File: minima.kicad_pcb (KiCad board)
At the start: 2 copper layers, 84 x 60 mm, 40 parts, among them J1 output, J2 input, J3 powersupply, U1 LM1875

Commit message: Release version v1.1
Signed-off-by: Nenad Radulovic <nenad.b.radulovic@gmail.com>
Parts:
- moved LOGO1 33.9 mm to (110.5, 64.2), turned to 270 degrees
- moved J2 13.1 mm to (120.2, 97.2)
- moved C4 11.2 mm to (117.0, 69.3)
- moved C14 9.86 mm to (120.8, 82.0)
- moved R11 9.86 mm to (113.2, 85.2)
- moved R12 9.86 mm to (113.2, 78.8)
- moved C13 9.86 mm to (120.8, 88.3)
- moved R10 9.86 mm to (120.8, 91.5)
- moved J1 3.36 mm to (165.2, 99.8)
- moved L1 3.24 mm to (155.1, 58.5)
- moved R6 3.18 mm to (170.3, 50.2)
- moved MK1 3.00 mm to (112.6, 99.7)
- moved MK2 3.00 mm to (112.6, 51.7)
- moved MK3 3.00 mm to (178.6, 51.7)
- moved MK4 3.00 mm to (178.6, 99.7)
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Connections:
- J2 pad 2: GNDPWR -> /Input amplifier/sgnd
- J2 pad 3: /Input amplifier/sgnd -> GNDPWR
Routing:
- net /Input amplifier/sgnd: track 61.4 -> 83.2 mm
- net Net-(C10-Pad1): track 102.0 -> 112.4 mm
- net VCC: track 52.3 -> 42.0 mm, vias 0 -> 1
- net Net-(C4-Pad1): track 19.2 -> 10.8 mm
- net /Input amplifier/inp: track 5.91 -> 10.8 mm
- net VEE: track 56.0 -> 53.5 mm
- net /Power amplifier/inp: track 21.9 -> 24.1 mm
- net GNDPWR: track 110.7 -> 109.0 mm
- net /Power amplifier/spkhot: track 53.6 -> 54.6 mm
- net Net-(C7-Pad1): track 10.1 -> 11.1 mm
- net Net-(C3-Pad1): track 4.45 -> 3.81 mm
- net Net-(C2-Pad1): track 4.38 -> 3.81 mm
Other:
- board size 84 x 60 mm -> 78 x 60 mm
- board text added: "+|SG|G"
- board text added: "20180801-1.1"
- board text added: "Minima V1.1"
- board text removed: "+|G|SG"
- board text removed: "01.08.2018 1.0"
- board text removed: "Minima V1.0"

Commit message: Switching to single sch sheet 1
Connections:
- net /Input amplifier/inp renamed /inp
- net /Input amplifier/sgnd renamed /sgnd
- net /Power amplifier/inp renamed Net-(C14-Pad1)
- net /Power amplifier/spkhot renamed /spkhot

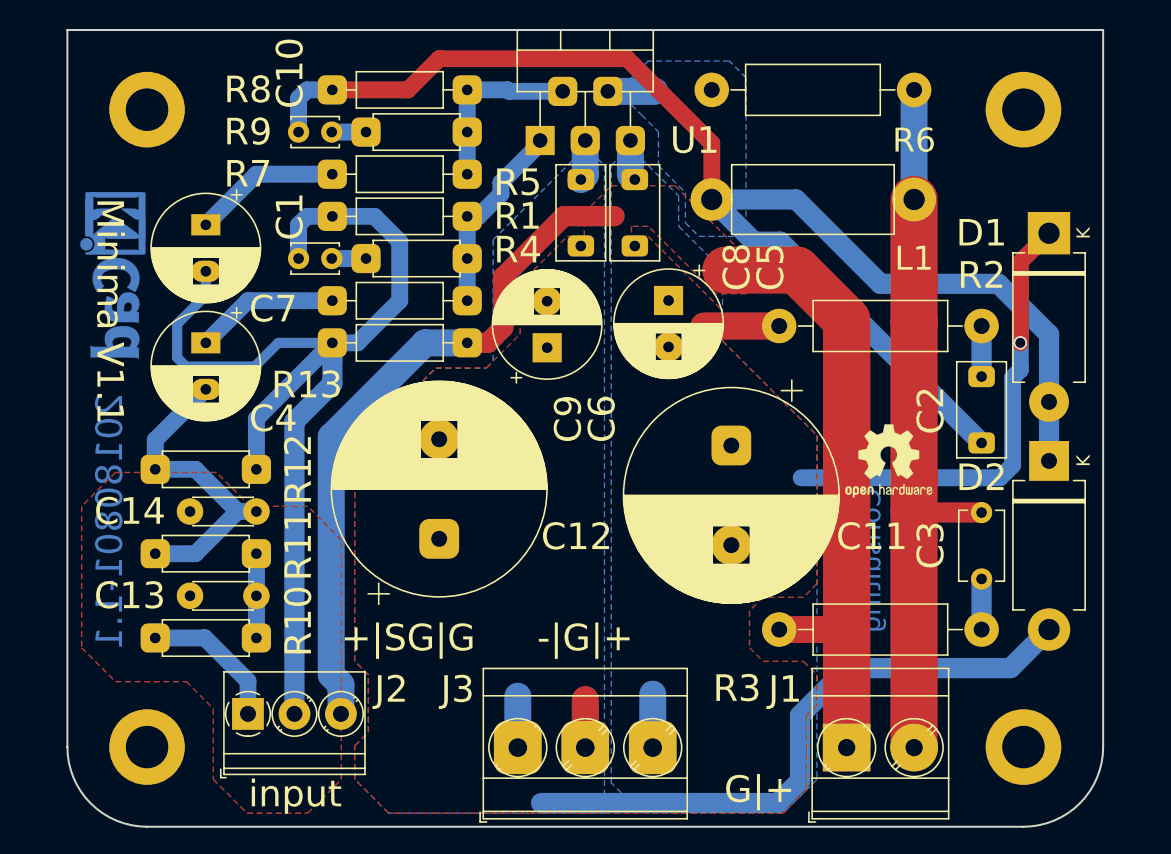
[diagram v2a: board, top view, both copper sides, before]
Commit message: Removed sheets
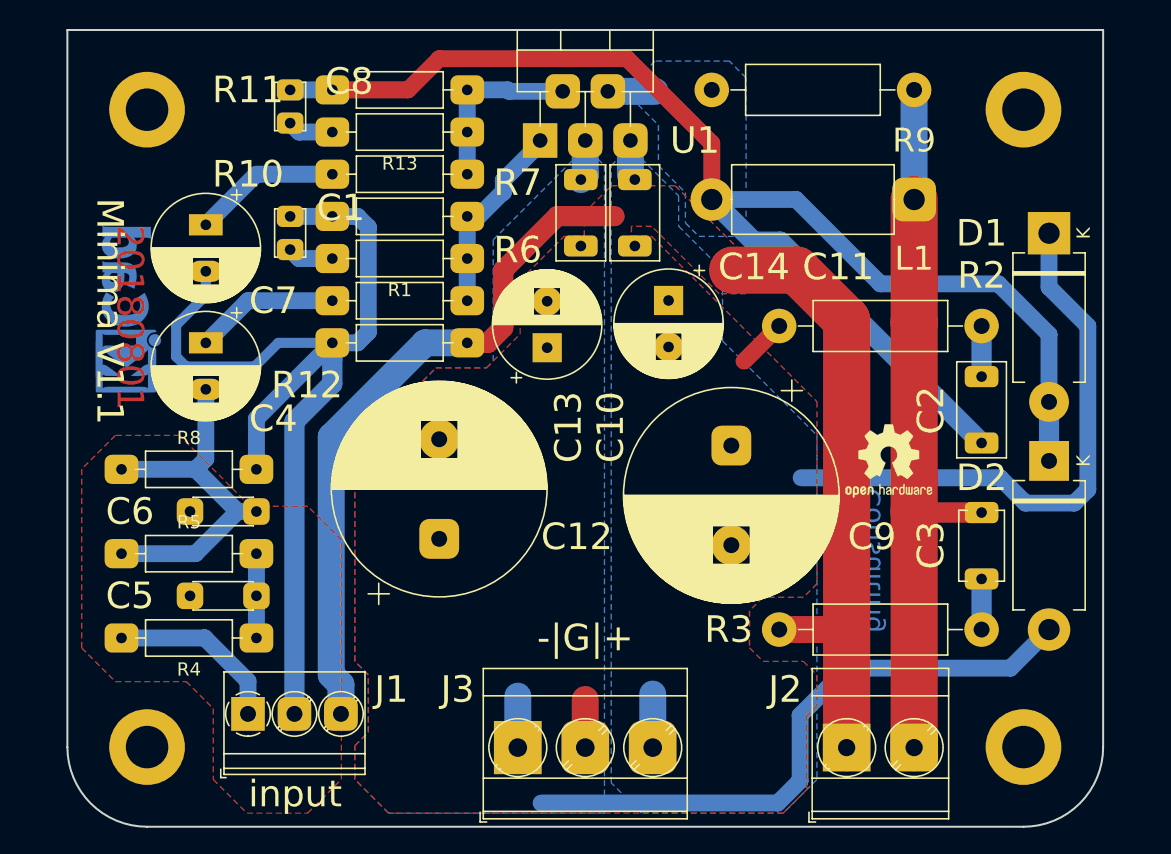
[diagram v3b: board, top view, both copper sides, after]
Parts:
- removed the C10 at (124.0, 53.4)
- removed the R10 at (120.8, 91.5)
- removed the R11 at (113.2, 85.2)
- removed the R12 at (113.2, 78.8)
- removed the R9 at (136.7, 53.4)
- added C8: 15p, Capacitor_THT:C_Disc_D3.4mm_W2.1mm_P2.50mm, F.Cu at (123.3, 50.2)
- added R13: 1k6, Resistor_THT:R_Axial_DIN0207_L6.3mm_D2.5mm_P10.16mm_Horizontal, F.Cu at (136.7, 53.4)
- added R4: 100, Resistor_THT:R_Axial_DIN0207_L6.3mm_D2.5mm_P10.16mm_Horizontal, F.Cu at (120.8, 91.5)
- added R5: 100, Resistor_THT:R_Axial_DIN0207_L6.3mm_D2.5mm_P10.16mm_Horizontal, F.Cu at (110.6, 85.2)
- added R8: 100k, Resistor_THT:R_Axial_DIN0207_L6.3mm_D2.5mm_P10.16mm_Horizontal, F.Cu at (110.6, 78.8)
- R1: footprint Resistor_THT:R_Axial_DIN0207_L6.3mm_D2.5mm_P7.62mm_Horizontal -> Resistor_THT:R_Axial_DIN0207_L6.3mm_D2.5mm_P10.16mm_Horizontal
- moved C1 3.24 mm to (123.3, 59.8), turned to 270 degrees
- moved LOGO1 2.54 mm to (110.6, 66.7), turned to 90 degrees
- renumbered C6 to C10, C5 to C11, C9 to C13, C8 to C14, C13 to C5, C14 to C6, C11 to C9, J2 to J1, J1 to J2, R7 to R10, R8 to R11, R13 to R12, R4 to R6, R5 to R7, R6 to R9
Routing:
- net VCC: track 42.0 -> 50.4 mm, vias 1 -> 0
- net /sgnd: track 83.2 -> 78.4 mm
- net Net-(C4-Pad2): track 24.1 -> 27.9 mm
- net Net-(C8-Pad2): track 0.00 -> 3.45 mm
- net Net-(C10-Pad2): track 2.58 -> 0.00 mm
- net /inp: track 10.8 -> 13.4 mm
- net Net-(C2-Pad2): track 112.4 -> 110.2 mm
- net GNDPWR: track 109.0 -> 106.8 mm
- net Net-(C1-Pad2): track 2.58 -> 3.45 mm
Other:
- board text added: "20180801"
- board text removed: "+|SG|G"
- board text removed: "20180801-1.1"
- board text removed: "G|+"

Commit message: Wider pads and some final touches to silkscreen.
Signed-off-by: Nenad Radulovic <nenad.b.radulovic@gmail.com>
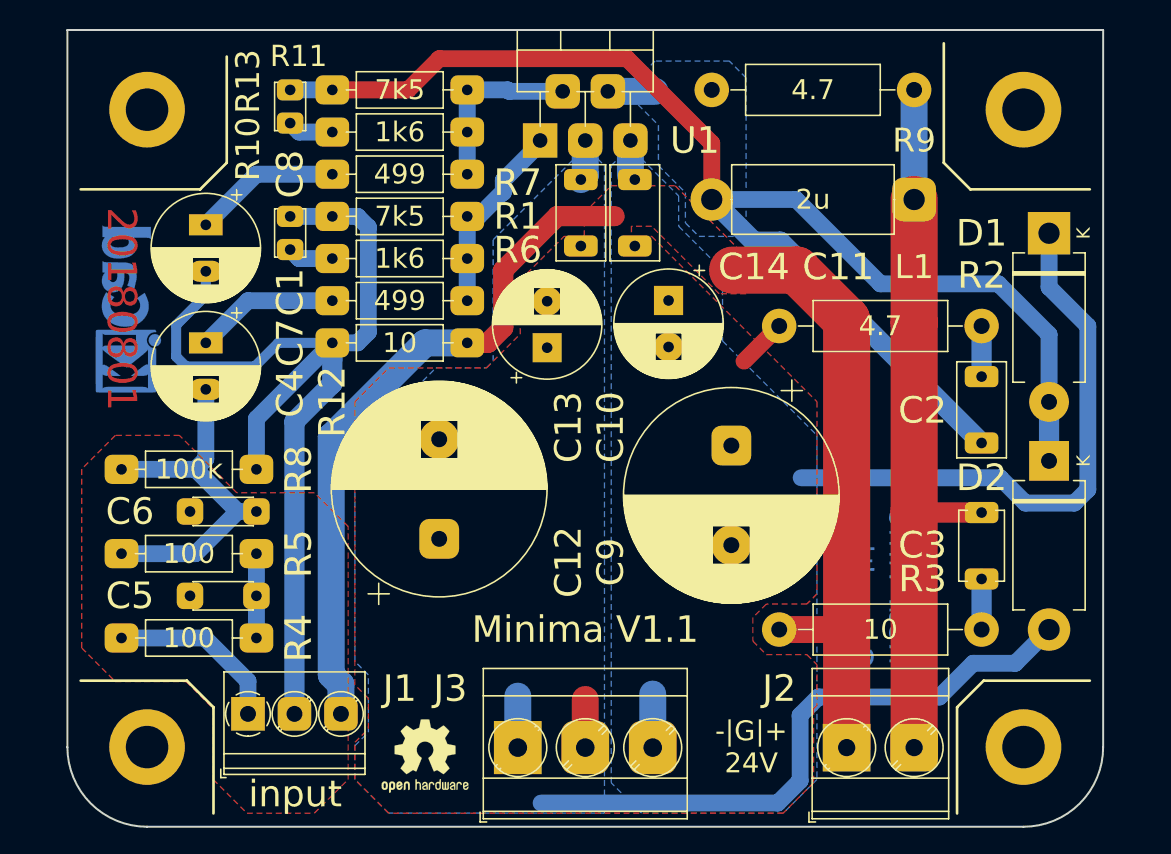
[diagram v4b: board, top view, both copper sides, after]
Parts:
- moved LOGO2 41.4 mm to (133.5, 100.4)
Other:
- board text added: "-|G|+ 24V"
- board text removed: "-|G|+"
